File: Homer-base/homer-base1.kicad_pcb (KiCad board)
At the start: 2 copper layers, 19 parts

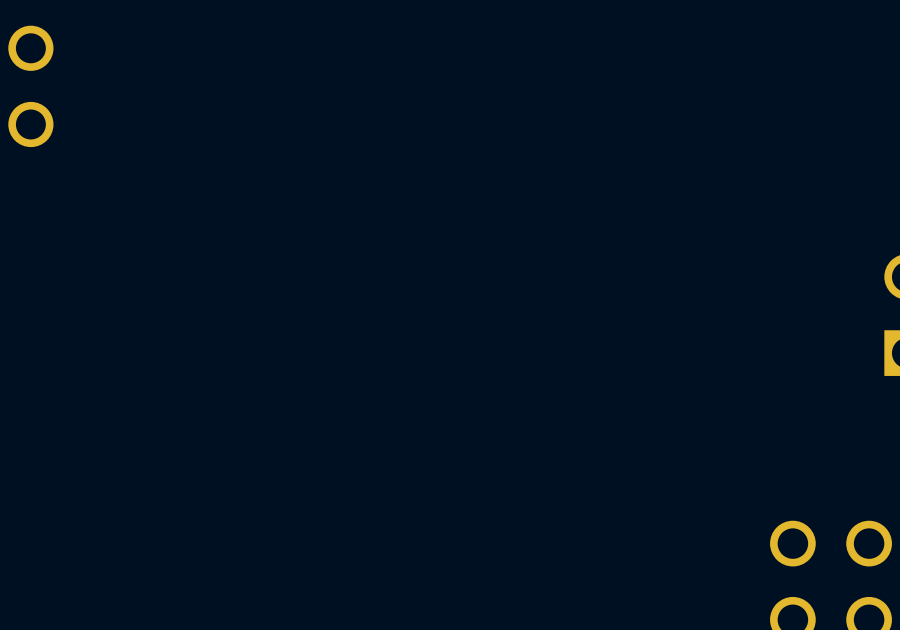
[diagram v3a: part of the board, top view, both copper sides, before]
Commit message: Power revision and add ina219 sensor
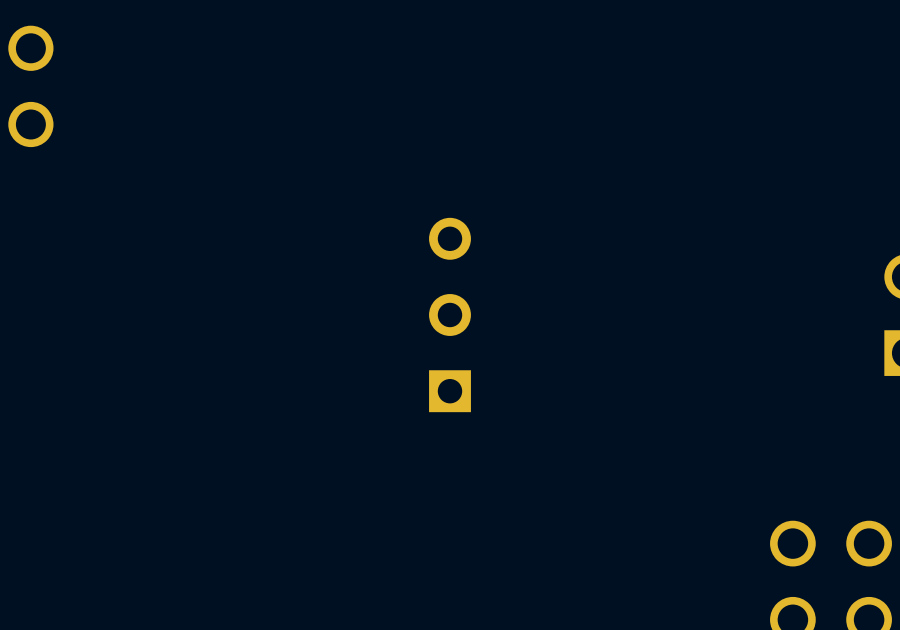
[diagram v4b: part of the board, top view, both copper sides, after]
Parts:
- added ?: Val**, SIL-3, F.Cu at (50.8, -861.1)
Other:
- board text added: "(3,6)"
- board text added: "3,3"
- board text added: "3,6V,NC,NC,NC,B4,B2,SCA,BKL"
- board text added: "GND,NC,NC,B5,B3,B1,SCL,RST"
- board text added: "NC,NC,NC,NC,NC,NC,AD0,SCL"
- board text added: "NC,NC,NC,NC,NC,NC,AD1,SCA"
- board text added: "VREF"
- board text removed: "3,6V,NC,NC,NC,B4,B2,SCA,RST"
- board text removed: "GND,NC,NC,B5,B3,B1,SCL,BL"
- board text removed: "NC,NC,NC,NC,NC,NC,NC,SCA"
- board text removed: "NC,NC,NC,NC,NC,NC,NC,SCL"
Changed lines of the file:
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@@
 (kicad_pcb (version 3) (host pcbnew "(22-Jun-2014 BZR 4027)-stable")
   (general
-    (links 56)
+    (links 0)
     (no_connects 56)
     (area -31.03245 -878.940001 169.316401 -756.819999)
     (thickness 1.6)
-    (drawings 36)
+    (drawings 39)
     (tracks 0)
     (zones 0)
-    (modules 19)
+    (modules 20)
     (nets 23)
   )
@@
     )
   )
-  (gr_text NC,NC,NC,NC,NC,NC,NC,SCL (at 27.94 -875.03) (layer "Serigrafia Fronte")
-    (effects (font (size 1.5 1.5) (thickness 0.3)))
-  )
-  (gr_text NC,NC,NC,NC,NC,NC,NC,SCA (at 27.94 -862.33) (layer "Serigrafia Fronte")
+  (module SIL-3 (layer "Rame Fronte")
+    (at 50.8 -861.06 90)
+    (descr "Connecteur 3 pins")
+    (tags "CONN DEV")
+    (fp_text reference "" (at 0 -2.54 90) (layer "Serigrafia Fronte")
+      (effects (font (size 1.7907 1.07696) (thickness 0.26924)))
+    )
+    (fp_text value Val** (at 0 -2.54 90) (layer "Serigrafia Fronte") hide
+      (effects (font (size 1.524 1.016) (thickness 0.3048)))
+    )
+    (fp_line (start -3.81 1.27) (end -3.81 -1.27) (layer "Serigrafia Fronte") (width 0.3048))
+    (fp_line (start -3.81 -1.27) (end 3.81 -1.27) (layer "Serigrafia Fronte") (width 0.3048))
+    (fp_line (start 3.81 -1.27) (end 3.81 1.27) (layer "Serigrafia Fronte") (width 0.3048))
+    (fp_line (start 3.81 1.27) (end -3.81 1.27) (layer "Serigrafia Fronte") (width 0.3048))
+    (fp_line (start -1.27 -1.27) (end -1.27 1.27) (layer "Serigrafia Fronte") (width 0.3048))
+    (pad 1 thru_hole rect (at -2.54 0 90) (size 1.397 1.397) (drill 0.8128)
+      (layers *.Cu *.Mask "Serigrafia Fronte")
+    )
+    (pad 2 thru_hole circle (at 0 0 90) (size 1.397 1.397) (drill 0.8128)
+      (layers *.Cu *.Mask "Serigrafia Fronte")
+    )
+    (pad 3 thru_hole circle (at 2.54 0 90) (size 1.397 1.397) (drill 0.8128)
+      (layers *.Cu *.Mask "Serigrafia Fronte")
+    )
+  )
+  (gr_text 3,3 (at 55.88 -858.52) (layer "Serigrafia Fronte")
+    (effects (font (size 1.5 1.5) (thickness 0.3)))
+  )
+  (gr_text "(3,6)" (at 55.88 -863.6) (layer "Serigrafia Fronte")
+    (effects (font (size 1.5 1.5) (thickness 0.3)))
+  )
+  (gr_text VREF (at 55.88 -861.06) (layer "Serigrafia Fronte")
+    (effects (font (size 1.5 1.5) (thickness 0.3)))
+  )
+  (gr_text NC,NC,NC,NC,NC,NC,AD0,SCL (at 27.94 -875.03) (layer "Serigrafia Fronte")
+    (effects (font (size 1.5 1.5) (thickness 0.3)))
+  )
+  (gr_text NC,NC,NC,NC,NC,NC,AD1,SCA (at 27.94 -862.33) (layer "Serigrafia Fronte")
     (effects (font (size 1.5 1.5) (thickness 0.3)))
   )
@@
     (effects (font (size 1.5 1.5) (thickness 0.3)))
   )
-  (gr_text 3,6V,NC,NC,NC,B4,B2,SCA,RST (at 25.4 -844.55) (layer "Serigrafia Fronte")
-    (effects (font (size 1.5 1.5) (thickness 0.3)))
-  )
-  (gr_text GND,NC,NC,B5,B3,B1,SCL,BL (at 25.4 -857.25) (layer "Serigrafia Fronte")
-    (effects (font (size 1.5 1.5) (thickness 0.3)))
-  )
+  (gr_text 3,6V,NC,NC,NC,B4,B2,SCA,BKL (at 25.4 -844.55) (layer "Serigrafia Fronte")
+    (effects (font (size 1.5 1.5) (thickness 0.3)))
+  )
+  (gr_text GND,NC,NC,B5,B3,B1,SCL,RST (at 25.4 -857.25) (layer "Serigrafia Fronte")
+    (effects (font (size 1.5 1.5) (thickness 0.3)))
+  )

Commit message: Fix Power schematics
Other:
- board text added: "3,3V,NC,NC,NC,B4,B2,SCA,BKL"
- board text removed: "3,6V"
- board text removed: "3,6V GIALLO/BLU"
- board text removed: "3,6V,NC,NC,NC,B4,B2,SCA,BKL"
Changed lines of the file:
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@@
 (kicad_pcb (version 3) (host pcbnew "(22-Jun-2014 BZR 4027)-stable")
   (general
-    (links 0)
+    (links 56)
     (no_connects 56)
     (area -31.03245 -878.940001 169.316401 -756.819999)
     (thickness 1.6)
-    (drawings 39)
+    (drawings 37)
     (tracks 0)
     (zones 0)
@@
     (effects (font (size 1.5 1.5) (thickness 0.3)))
   )
-  (gr_text 3,6V (at -7.62 -842.01) (layer "Serigrafia Fronte")
-    (effects (font (size 1.5 1.5) (thickness 0.3)))
-  )
   (gr_text 3,3V (at -7.62 -847.09) (layer "Serigrafia Fronte")
     (effects (font (size 1.5 1.5) (thickness 0.3)))
@@
     (effects (font (size 1.5 1.5) (thickness 0.3)))
   )
-  (gr_text "3,6V GIALLO/BLU" (at 30.48 -820.42) (layer "Serigrafia Fronte")
-    (effects (font (size 1.5 1.5) (thickness 0.3)))
-  )
   (gr_text 1 (at 40.64 -853.44) (layer "Serigrafia Fronte")
     (effects (font (size 1.5 1.5) (thickness 0.3)))
@@
     (effects (font (size 1.5 1.5) (thickness 0.3)))
   )
-  (gr_text 3,6V,NC,NC,NC,B4,B2,SCA,BKL (at 25.4 -844.55) (layer "Serigrafia Fronte")
-    (effects (font (size 1.5 1.5) (thickness 0.3)))
-  )
+  (gr_text 3,3V,NC,NC,NC,B4,B2,SCA,BKL (at 25.4 -844.55) (layer "Serigrafia Fronte")
+    (effects (font (size 1.5 1.5) (thickness 0.3)))
+  )
